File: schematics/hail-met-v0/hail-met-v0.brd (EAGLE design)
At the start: 77.1 x 61 mm, 87 parts, among them IC1 MCP73871, J1 AVR_SPI_PRG_6PTH, U1 ATMEGA328P, Y1 16MHZ

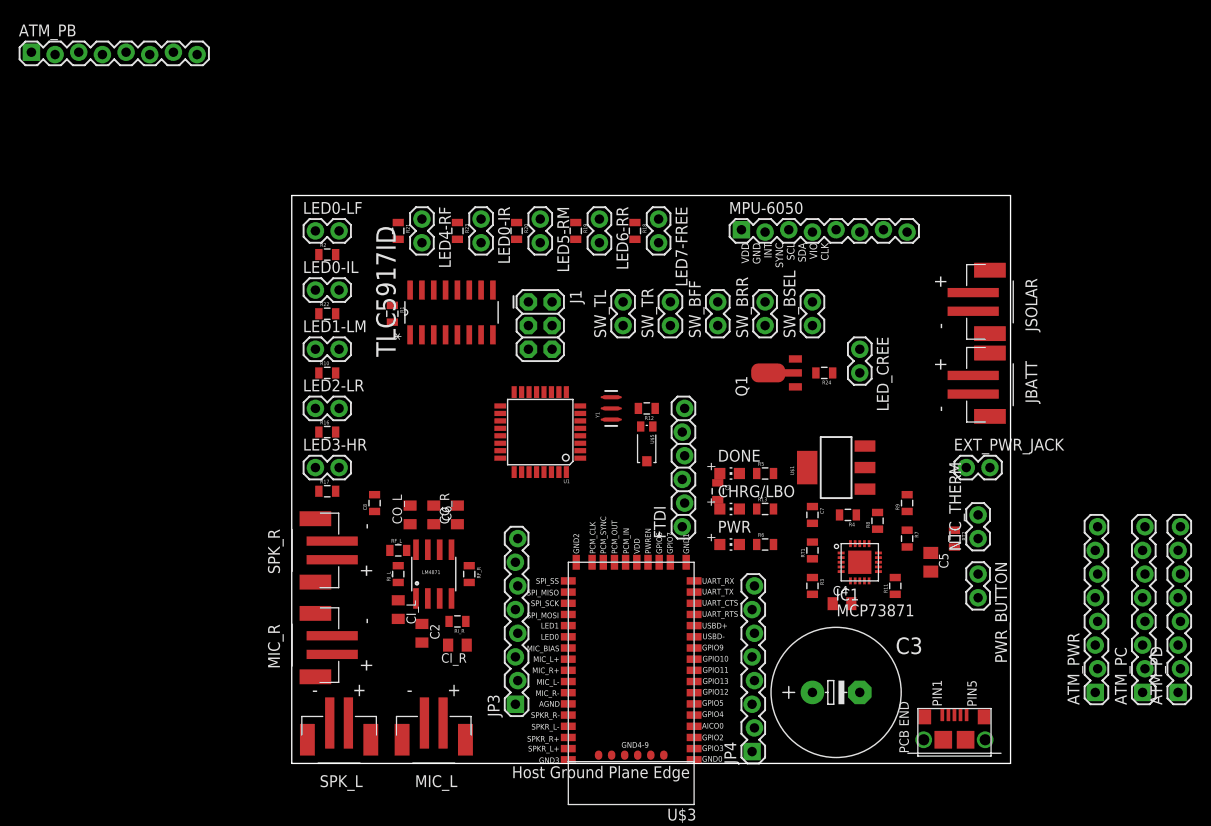
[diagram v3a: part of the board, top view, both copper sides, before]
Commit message: finished initial schematic and routing, updated software pin assignment
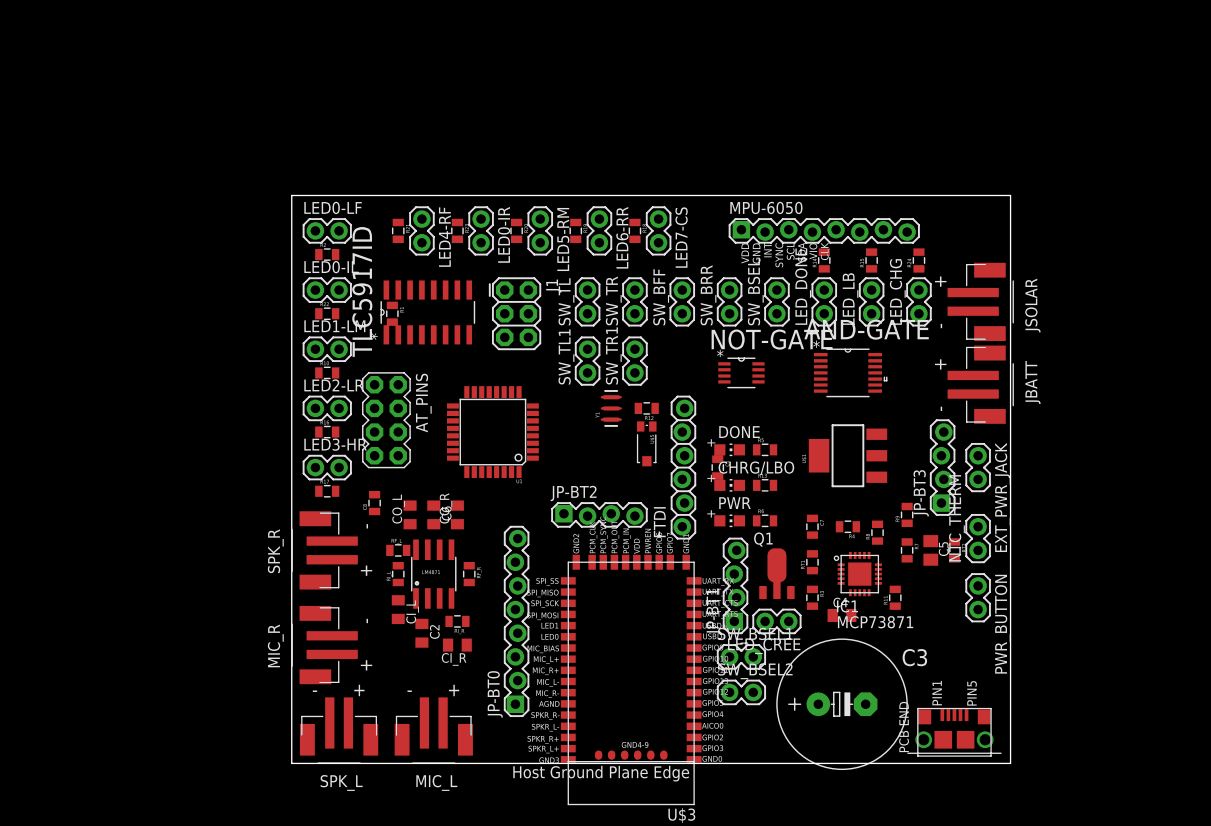
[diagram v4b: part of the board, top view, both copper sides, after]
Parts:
- removed ATM_PB, ATM_PC, ATM_PD, ATM_PWR, JP4: (no value), SparkFun-Connectors:1X08_LOCK
- added AND-GATE: SN74ALVC08PWR, Texas Instruments_By_element14_Batch_1:SOP65P640X120-14N
- added AT_PINS: M04X2, SparkFun-Connectors:2X4
- added JP-BT1, JP-BT2, JP-BT3: (no value), SparkFun-Connectors:1X04_LOCK
- added LED_CHG, LED_DONE, LED_LB, SW_BSEL1, SW_BSEL2, SW_TL1, SW_TR1: M02PTH, SparkFun-Connectors:1X02
- added NOT-GATE: SN74LVC3G14DCTR, Texas Instruments_By_element14_Batch_1:SOP65P400X130-8N
- added R14, R15: (no value), SparkFun-Passives:0805
- moved LED_CREE 30.2 mm to (53.3, 15.2), turned to 180 degrees
- moved Q1 21.6 mm to (52.1, 20.3), turned to 0 degrees
- moved R24 15.8 mm to (67.3, 54.0), turned to 90 degrees
- moved U1 5.08 mm to (21.6, 35.6)
- moved SW_BFF 4.02 mm to (41.9, 48.3)
- moved SW_BSEL 4.02 mm to (52.1, 48.3)
- moved SW_TL 4.02 mm to (31.8, 48.3)
- moved SW_TR 4.02 mm to (36.8, 48.3)
- moved SW_BRR 4.02 mm to (47.0, 48.3)
- moved J1 2.84 mm to (22.9, 50.8)
- moved DONE 2.54 mm to (47.0, 33.7)
- moved R5 2.54 mm to (50.8, 33.7)
- moved C1 2.54 mm to (45.7, 31.8)
- moved CHRG/LBO 2.54 mm to (47.0, 29.8)
- moved PWR 2.54 mm to (47.0, 26.0)
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- renumbered JP3 to JP-BT0, LED7-FREE to LED7-CS
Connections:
- net CHG_PWR renamed N$29
- removed net A: U1.24
- removed net B: U1.25
- removed net BT_DISC: U1.2
- removed net BT_GPIO10: JP4.8, U$3.GPIO10
- removed net BT_GPIO2: JP4.1
- removed net BT_GPIO5: JP4.4, U$3.GPIO5
- removed net BT_GPIO9: JP4.7
- removed net BT_PAIR: U1.11
- removed net C: U1.26
- removed net N$15: ATM_PC.1, ATM_PD.1
- removed net N$16: ATM_PC.2, ATM_PD.2
- removed net N$23: DONE.A, R5.1
- removed net N$26: ATM_PC.3, ATM_PD.3
- removed net N$32: ATM_PC.4, ATM_PD.4
- removed net N$34: U1.22
- removed net N$43: ATM_PC.5, ATM_PD.5, ATM_PWR.5
- removed net N$45: ATM_PC.6, ATM_PD.6, ATM_PWR.6
- removed net N$46: ATM_PC.7, ATM_PD.7, ATM_PWR.7
- removed net N$47: ATM_PC.8, ATM_PD.8, ATM_PWR.8
- removed net N$48: ATM_PB.1
- removed net N$49: ATM_PB.2
- removed net N$50: ATM_PB.3
- removed net N$51: ATM_PB.4
- removed net N$52: ATM_PB.5
- removed net N$53: ATM_PB.6
- removed net N$54: ATM_PB.7
- removed net N$55: ATM_PB.8
- removed net N$67: LED_CREE.2, R24.1
- removed net SW_BFF: SW_BFF.1
- removed net SW_BRR: SW_BRR.1
- removed net SW_BSEL: SW_BSEL.1
- new net ADC6: AT_PINS.2, U1.19
- new net ADC7: AT_PINS.4, U1.22
- new net BT_NEXT: SW_BSEL1.1, U$3.GPIO11
- new net BT_PLAY: SW_BSEL.1, U$3.GPIO13
- new net BT_PREV: SW_BSEL2.1, U$3.GPIO12
- new net BT_USBD+: JP-BT1.3, U$3.USBD+
- new net BT_USBD-: JP-BT1.2, U$3.USBD-
- new net BT_VOL_DN: SW_BRR.1, U$3.GPIO10
- new net BT_VOL_UP: SW_BFF.1, U$3.GPIO5
- new net CHG_CHARGING: AND-GATE.11, LED_CHG.1
- new net CHG_LOWBATT: AND-GATE.8, LED_LB.1
- new net CHG_PG: AND-GATE.10, NOT-GATE.6, PWR.A, R6.1
- new net CHG_STAT2: AND-GATE.5, DONE.A, NOT-GATE.3, R5.1
- new net N$20: CHRG/LBO.C, IC1.8
- new net N$28: DONE.C, IC1.7
- new net N$30: LED_CHG.2, R24.1
- new net PC1: AT_PINS.3, U1.24
- new net PC2: AT_PINS.5, U1.25
- new net PC3: AT_PINS.7, U1.26
- new net STAT12: AND-GATE.12, AND-GATE.6, AND-GATE.9
- new net SW_BT_DISC: SW_TL1.1, U1.2
- new net SW_CALL: SW_TR1.1
- new net ~CHG_PG: AND-GATE.13, NOT-GATE.2
- new net ~CHG_STAT1: AND-GATE.4, NOT-GATE.7
- new net ~CHG_STAT2: AND-GATE.2, NOT-GATE.5
- net 3.3V: now also AND-GATE.14, AT_PINS.1, JP-BT2.4, NOT-GATE.8, R13.2, R5.2, R6.2
- net AMB_IN: now also U1.23; no longer U1.19
- net BT_CONN: now also U1.11; no longer U1.9
- net BT_GPIO3: now also JP-BT1.1; no longer JP4.2
- net BT_GPIO4: now also JP-BT2.1; no longer JP4.3
- net BT_GPIO6: now also JP-BT2.2; no longer JP4.5
- net BT_GPIO7: now also JP-BT2.3; no longer JP4.6
- net CHG_DONE: now also AND-GATE.3, LED_DONE.1; no longer DONE.C, IC1.7
- net CHG_STAT1: now also AND-GATE.1, CHRG/LBO.A, NOT-GATE.1, R13.1; no longer CHRG/LBO.C, IC1.8
- net CHG_VOUT: now also JP-BT3.1; no longer ATM_PWR.1, C7.1, U$1.3
- net EXT_5V: now also JP-BT3.3; no longer ATM_PWR.3
- net GND: now also AND-GATE.7, AT_PINS.6, AT_PINS.8, JP-BT1.4, JP-BT3.4, NOT-GATE.4, R14.2, R15.2, R24.2, SW_BSEL1.2, SW_BSEL2.2, SW_TL1.2, SW_TR1.2; no longer ATM_PWR.4
- net LED_CREE: now also U1.9; no longer U1.23
- net N$19: now also LED_CREE.2; no longer R24.2
- net N$22: now also LED_DONE.2, R14.1; no longer CHRG/LBO.A, R13.1
- net N$24: now also LED_LB.2, R15.1; no longer PWR.A, R6.1
- net VCHG: no longer R13.2, R5.2, R6.2
- net VIN: now also C7.1, JP-BT3.2, U$1.3; no longer ATM_PWR.2

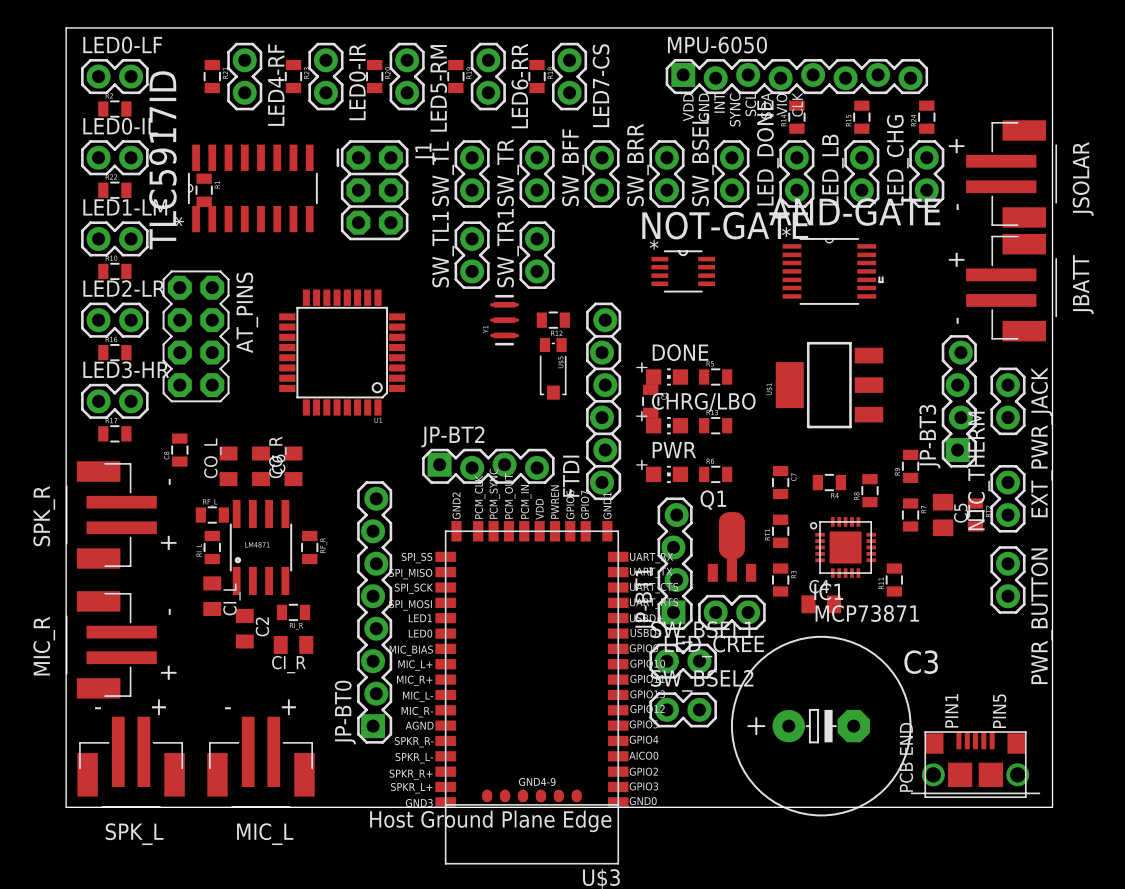
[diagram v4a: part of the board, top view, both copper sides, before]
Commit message: added some power planes
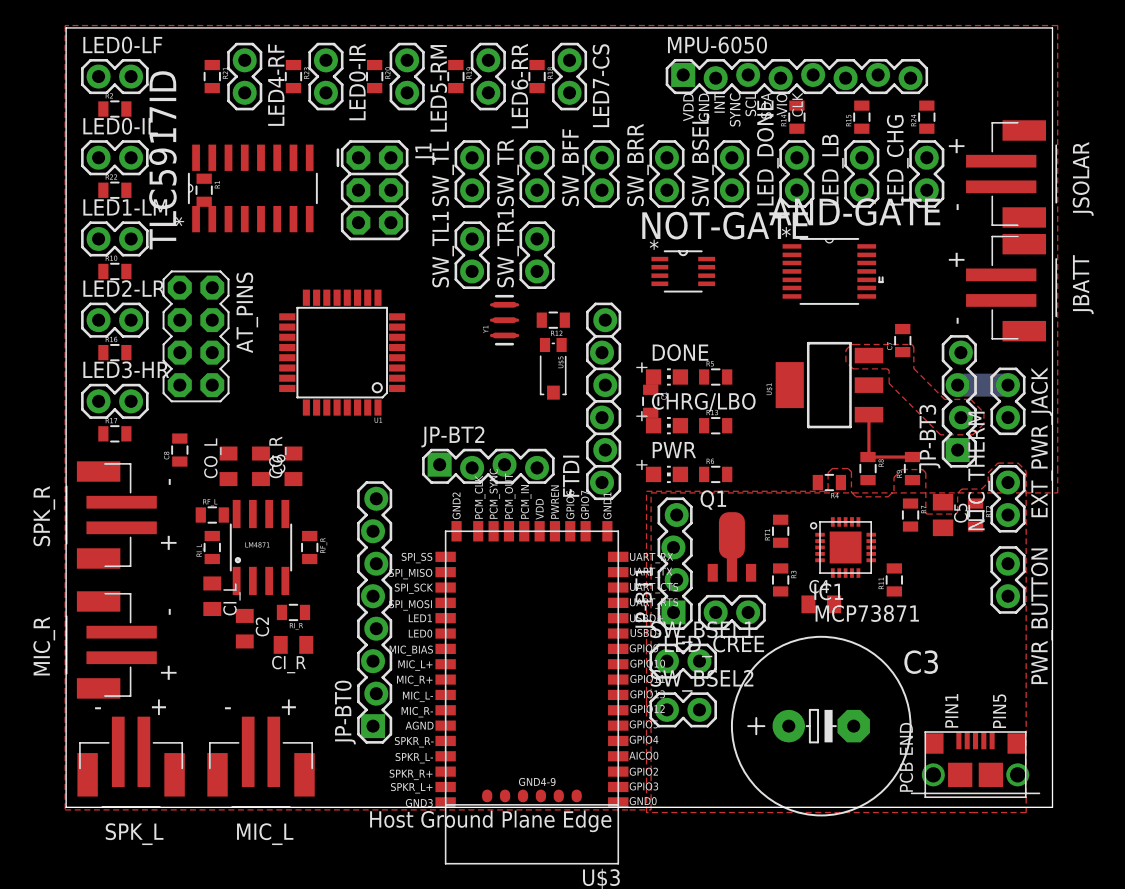
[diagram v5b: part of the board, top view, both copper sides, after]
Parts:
- moved C7 14.6 mm to (65.4, 36.5), turned to 90 degrees
- moved R8 1.73 mm to (62.7, 26.5), turned to 270 degrees
- moved R9 0.23 mm to (66.2, 26.5)
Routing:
- net N$4: track 0.00 -> 6.83 mm
- net EXT_5V: track 0.00 -> 3.94 mm
- added copper zone on layer 1, net 3.3V
- added copper zone on layer 1, net GND
- added copper zone on layer 1, net VIN

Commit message: routing pcb
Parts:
- removed JP-BT0: (no value), SparkFun-Connectors:1X08_LOCK
- removed SW_TL1, SW_TR1: M02PTH, SparkFun-Connectors:1X02
- added D2: (no value), adafruit:SOD-123
- added LED_BTCONN, SW_CALL, SW_DISC: M02PTH, SparkFun-Connectors:1X02
- added R25: (no value), SparkFun-Passives:0805
- added R26, R27, R28: 1K, SparkFun-Passives:0805
- NOT-GATE: value SN74LVC3G14DCTR -> SN74AUP3G04DQER; device Texas Instruments_By_element14_Batch_1:SOP65P400X130-8N -> Texas Instruments_By_element14_Batch_1:SON35P100X140X40-8N
- R13, R5, R6: value 1K -> 10K
- moved C1 24.0 mm to (22.0, 28.2)
- moved R6 11.0 mm to (54.2, 36.5)
- moved MIC_R 10.9 mm to (6.40, 2.51), turned to 180 degrees
- moved SPK_L 10.5 mm to (2.54, 12.7), turned to 90 degrees
- moved PWR 9.86 mm to (53.2, 33.7), turned to 0 degrees
- moved NOT-GATE 6.19 mm to (53.6, 38.9), turned to 180 degrees
- moved R5 5.84 mm to (46.3, 37.4), turned to 90 degrees
- moved CHRG/LBO 5.01 mm to (50.3, 33.6), turned to 0 degrees
- moved R21 4.97 mm to (16.2, 55.9)
- moved R8 2.87 mm to (60.7, 28.5), turned to 180 degrees
- moved R1 2.49 mm to (8.38, 47.7)
- moved AND-GATE 2.47 mm to (57.2, 42.1)
- moved R13 2.02 mm to (48.8, 30.2), turned to 270 degrees
- moved R18 1.53 mm to (37.0, 55.6)
- moved R20 1.35 mm to (24.2, 55.8)
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- renumbered SW_BFF to SW_VUP, SW_BRR to SW_VDN, SW_BSEL to SW_PLAY, SW_BSEL1 to SW_NEXT, SW_BSEL2 to SW_PREV
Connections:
- removed net N$25: U1.20
- removed net N$28: DONE.C, IC1.7
- removed net N$29: IC1.6, PWR.C
- removed net N$73: CI_L.2, U$3.SPKR_L+
- removed net N$76: CI_R.2, U$3.SPKR_R+
- removed net PC3: AT_PINS.7, U1.26
- removed net SPKR_L-: JP-BT0.3
- removed net SPKR_R-: JP-BT0.4
- new net AREF: AT_PINS.3, U1.20
- new net N$15: D2.A, JSOLAR.2
- new net N$16: LED_BTCONN.2, R25.1
- new net N$23: PWR.A, R28.1
- net 3.3V: now also R26.2, R27.2, R28.2
- net BT_CONN: now also LED_BTCONN.1
- net CHG_PG: now also IC1.6, PWR.C; no longer PWR.A
- net CHG_STAT1: now also CHRG/LBO.C, IC1.8; no longer CHRG/LBO.A
- net CHG_STAT2: now also DONE.C, IC1.7; no longer DONE.A
- net GND: now also R25.2, SW_CALL.2, SW_DISC.2, U$3.AGND; no longer SW_TL1.2, SW_TR1.2
- net MIC_L+: no longer JP-BT0.8
- net MIC_L-: no longer JP-BT0.6
- net MIC_R+: no longer JP-BT0.7
- net MIC_R-: no longer JP-BT0.5
- net N$20: now also CHRG/LBO.A, R26.1; no longer CHRG/LBO.C, IC1.8
- net N$21: now also DONE.A, R27.1; no longer J1.2
- net N$80: now also D2.C; no longer JSOLAR.2
- net PC1: now also AT_PINS.5; no longer AT_PINS.3
- net PC2: now also AT_PINS.7; no longer AT_PINS.5
- net SPKR_L+: now also CI_L.2, U$3.SPKR_L+; no longer JP-BT0.1
- net SPKR_R+: now also CI_R.2, U$3.SPKR_R+; no longer JP-BT0.2
- net SW_BT_DISC: now also SW_DISC.1; no longer SW_TL1.1
- net SW_CALL: now also SW_CALL.1, U1.26; no longer SW_TR1.1
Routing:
- net GND: track 0.00 -> 33.2 mm, vias 0 -> 10
- net N$27: track 0.00 -> 18.9 mm
- net SPKR_R: track 0.00 -> 6.31 mm
- net CHG_STAT2: track 0.00 -> 1.86 mm
- net N$21: track 0.00 -> 1.38 mm
- net N$4: track 6.83 -> 7.50 mm
- added copper zone on layer 16, net GND

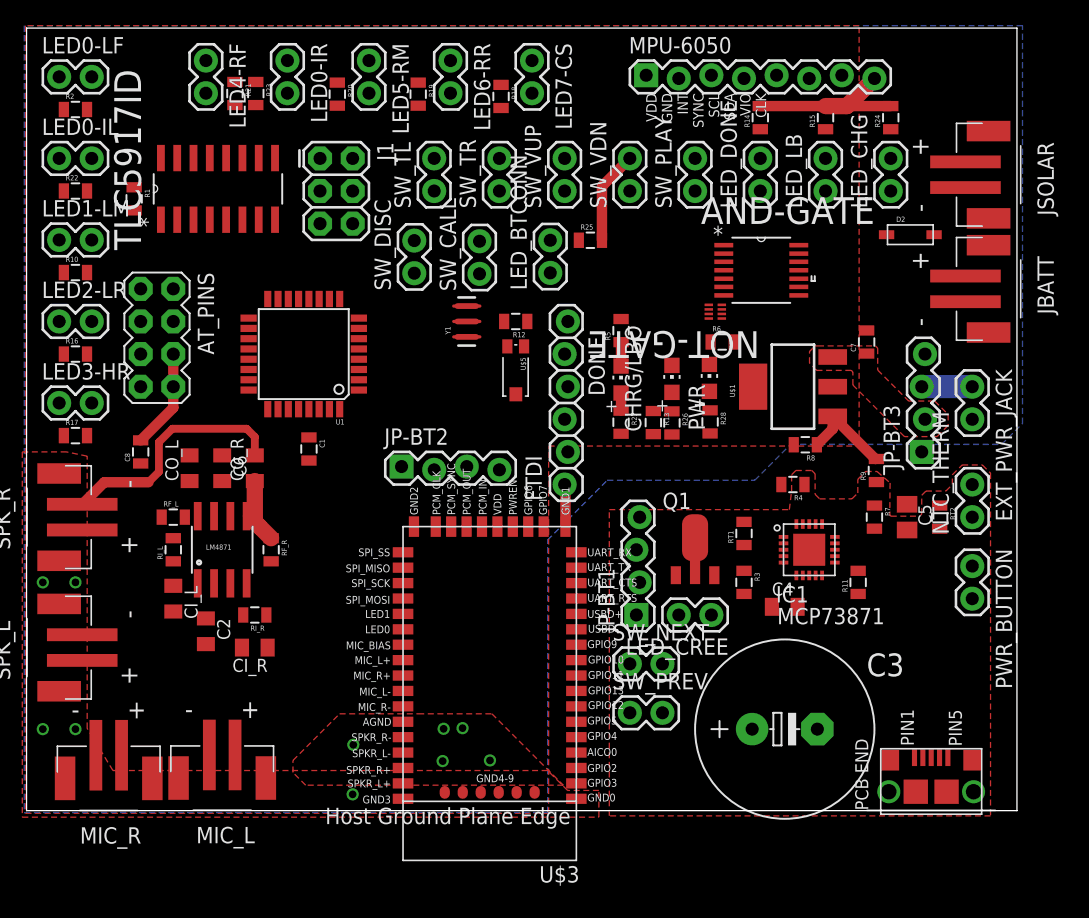
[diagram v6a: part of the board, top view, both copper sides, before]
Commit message: added to layout
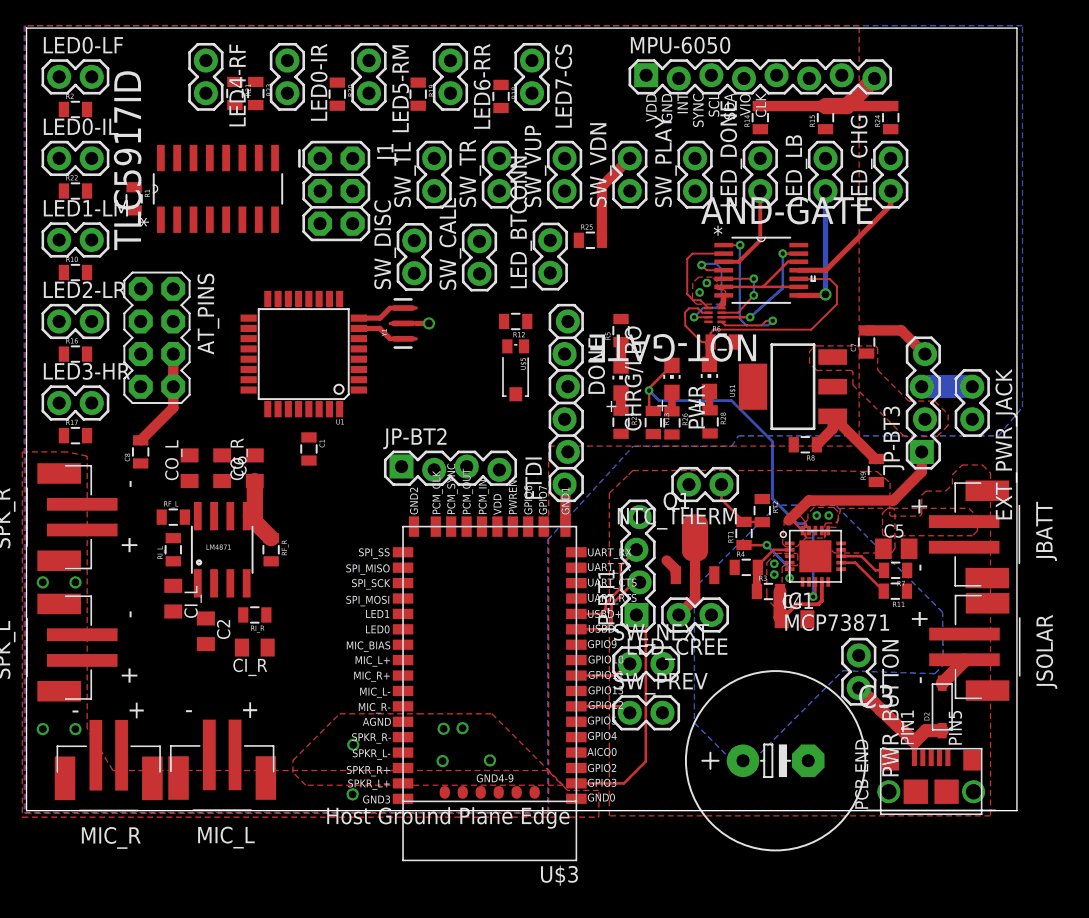
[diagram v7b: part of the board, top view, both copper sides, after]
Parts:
- moved D2 36.9 mm to (71.3, 8.08), turned to 90 degrees
- moved JSOLAR 36.8 mm to (74.9, 12.8)
- moved NTC_THERM 19.7 mm to (54.1, 25.4), turned to 180 degrees
- moved JBATT 19.1 mm to (74.8, 21.5)
- moved RT2 13.8 mm to (57.3, 23.4)
- moved PWR_BUTTON 11.3 mm to (64.8, 12.1)
- moved R4 7.40 mm to (56.1, 18.9), turned to 0 degrees
- moved Y1 4.96 mm to (29.3, 37.9)
- moved R7 4.46 mm to (67.7, 18.7), turned to 180 degrees
- moved R11 2.98 mm to (67.7, 17.1), turned to 180 degrees
- moved C5 2.60 mm to (67.7, 20.4), turned to 0 degrees
- moved C3 2.56 mm to (58.3, 3.89)
- moved R3 2.03 mm to (57.8, 17.1), turned to 0 degrees
- moved C4 1.23 mm to (59.8, 14.9)
- moved IC1 0.70 mm to (61.4, 19.8)
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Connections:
- removed net N$27: CO_R.2, SPK_R.2
- new net N$26: CO_R.2, SPK_R.1
- net GND: now also JBATT.2, SPK_L.2, SPK_R.2; no longer JBATT.1, SPK_L.1, SPK_R.1
- net MIC_L+: now also MIC_L.1; no longer MIC_L.2
- net MIC_L-: now also MIC_L.2; no longer MIC_L.1
- net MIC_R+: now also MIC_R.1; no longer MIC_R.2
- net MIC_R-: now also MIC_R.2; no longer MIC_R.1
- net N$14: now also SPK_L.1; no longer SPK_L.2
- net VBATT: now also JBATT.1; no longer JBATT.2
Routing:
- net CHG_STAT1: track 0.00 -> 44.8 mm, vias 0 -> 4
- net CHG_PG: track 0.00 -> 23.5 mm
- net N$27: track 18.9 -> 0.00 mm
- net BT_GPIO3: track 0.00 -> 17.8 mm
- net CHG_VOUT: track 0.00 -> 14.9 mm
- net CHG_CHARGING: track 0.00 -> 10.4 mm
- net CHG_LOWBATT: track 0.00 -> 10.2 mm, vias 0 -> 1
- net ~CHG_STAT1: track 0.00 -> 10.1 mm, vias 0 -> 2
- net N$80: track 0.00 -> 9.77 mm
- net ~CHG_PG: track 0.00 -> 9.57 mm, vias 0 -> 2
- net STAT12: track 0.00 -> 9.45 mm
- net BT_USBD+: track 0.00 -> 8.05 mm
- net GND: track 33.2 -> 41.1 mm, vias 10 -> 13
- net ~CHG_STAT2: track 0.00 -> 7.86 mm
- net VCHG: track 0.00 -> 7.40 mm, vias 0 -> 4
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- added copper zone on layer 1, net CHG_VOUT
- added copper zone on layer 1, net VBATT
- added copper zone on layer 1, net VCHG
- added copper zone on layer 16, net VCHG
